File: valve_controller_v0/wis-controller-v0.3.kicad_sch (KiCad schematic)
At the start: 45 parts, among them J3 USB_C_Receptacle_USB2.0, J5 SWD, J6 JST-2PH, Q1 DMG3415UQ-7, SW1 RESET, SW4 BOOT, U1 RAK3172, U10 BAT_Positive, U11 XKB5858-Z-F-75, U2 CH340E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

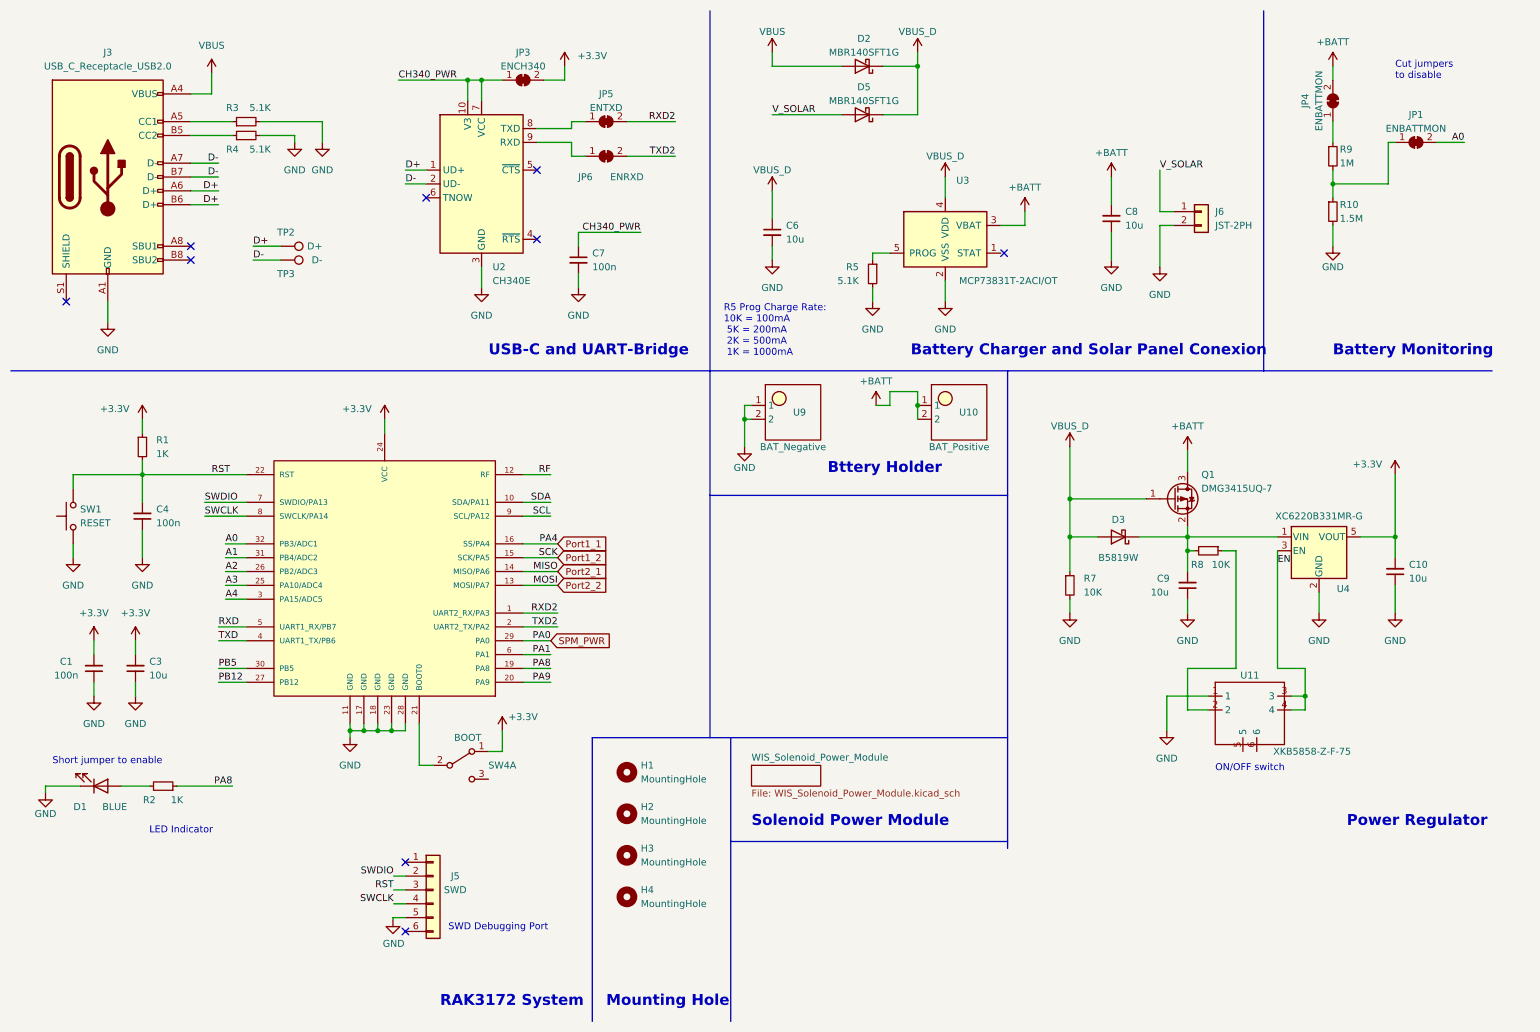
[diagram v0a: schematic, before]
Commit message: Replaced battery charger and battery holder
- Replaced battery charger to support the  new solar panel
- Replaced the battery holder by a plastic enclosure one
- Reconnected the on/off switch to avoid putting EN pin floating temporarly whne swithced
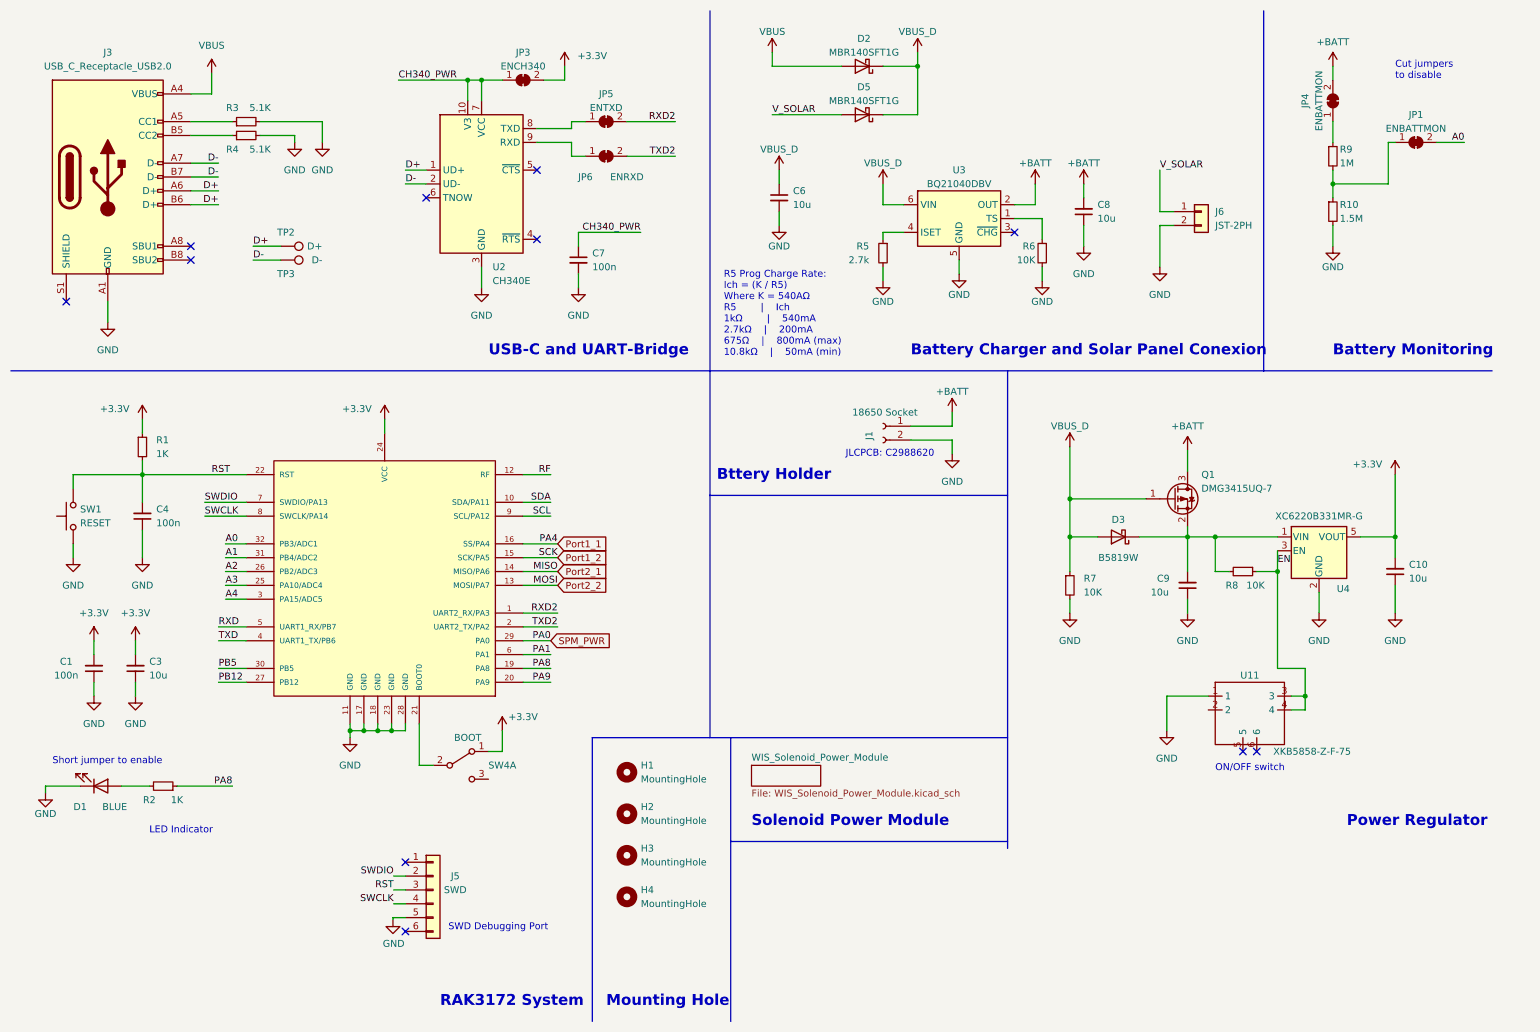
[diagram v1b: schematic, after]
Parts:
- removed U10: BAT_Positive, WIS_Solenoid_Power_module:Battery_holder_18650, symbol WISFLOW_Symbols:Battery_holder_side
- removed U3: MCP73831T-2ACI/OT, Package_TO_SOT_SMD:SOT-23-5, symbol Battery_Management:MCP73831-2-OT
- removed U9: BAT_Negative, WIS_Solenoid_Power_module:Battery_holder_18650, symbol WISFLOW_Symbols:Battery_holder_side
- added J1: 18650 Socket, Wisflow:18650_SMD, symbol Connector:Conn_01x02_Socket
- added R6: 10K, Resistor_SMD:R_0603_1608Metric, symbol Device:R_Small
- added U3: BQ21040DBV, Package_TO_SOT_SMD:SOT-23-6, symbol Battery_Management:BQ21040DBV
- R5: value 5.1K -> 2.7k
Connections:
- net +BATT: now also J1.1 (Pin_1), U3.2 (OUT)
- net EN: now also R8.1
- net GND: now also J1.2 (Pin_2), R6.2, U3.5 (GND)
- net VBUS_D: now also U3.6 (VIN)
- net at U11.2: no longer R8.1
- net at R5.1: now also U3.4 (ISET)
- new net: R6.1, U3.1 (TS)
- no-connect marks 9 -> 11
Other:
- note added: "JLCPCB: C2988620"
- note added: "R5 Prog Charge Rate: Ich = (K / R5) Where K = 540AΩ R5 | Ich 1kΩ | 540mA 2.7kΩ | 200mA 675Ω | 800mA (max) 10.8kΩ | 50mA (min)"
- note removed: "R5 Prog Charge Rate: 10K = 100mA 5K = 200mA 2K = 500mA 1K = 1000mA"
- moved on the sheet: C6, C8, R8

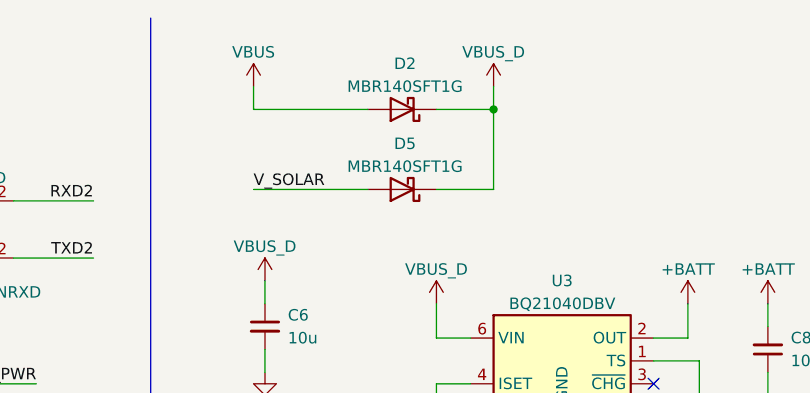
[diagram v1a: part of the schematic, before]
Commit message: Uniformized D2,D3 and D5
- Selected the same partnumber forD2, D3 and D5, all of the 1A and 40V.
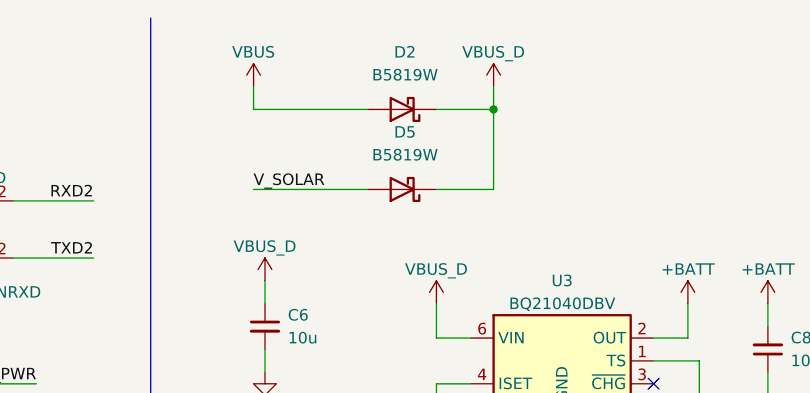
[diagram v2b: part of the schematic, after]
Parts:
- D2, D5: value MBR140SFT1G -> B5819W; footprint WIS_Solenoid_Power_module:D_MBR140SF -> Diode_SMD:D_SOD-123
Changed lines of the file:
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@@
 		(fields_autoplaced yes)
 		(property "Reference" "D2"
-			(at 169.2275 17.78 0)
-			(effects
-				(font
-					(size 1.27 1.27)
-				)
-			)
-		)
-		(property "Value" "MBR140SFT1G"
-			(at 169.2275 20.32 0)
-			(effects
-				(font
-					(size 1.27 1.27)
-				)
-			)
-		)
-		(property "Footprint" "WIS_Solenoid_Power_module:D_MBR140SF"
+			(at 169.2275 16.51 0)
+			(effects
+				(font
+					(size 1.27 1.27)
+				)
+			)
+		)
+		(property "Value" "B5819W"
+			(at 169.2275 19.05 0)
+			(effects
+				(font
+					(size 1.27 1.27)
+				)
+			)
+		)
+		(property "Footprint" "Diode_SMD:D_SOD-123"
 			(at 168.91 27.94 0)
 			(effects
@@
 		(fields_autoplaced yes)
 		(property "Reference" "D5"
-			(at 169.2275 26.67 0)
-			(effects
-				(font
-					(size 1.27 1.27)
-				)
-			)
-		)
-		(property "Value" "MBR140SFT1G"
-			(at 169.2275 29.21 0)
-			(effects
-				(font
-					(size 1.27 1.27)
-				)
-			)
-		)
-		(property "Footprint" "WIS_Solenoid_Power_module:D_MBR140SF"
+			(at 169.2275 25.4 0)
+			(effects
+				(font
+					(size 1.27 1.27)
+				)
+			)
+		)
+		(property "Value" "B5819W"
+			(at 169.2275 27.94 0)
+			(effects
+				(font
+					(size 1.27 1.27)
+				)
+			)
+		)
+		(property "Footprint" "Diode_SMD:D_SOD-123"
 			(at 168.91 36.83 0)
 			(effects

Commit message: Updated the 18650 battery holder
Changed the battery holder for the 18650 battery. Created new footprint and updated the PCB layout. Added cutouts for zip-ties
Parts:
- J1: footprint Wisflow:18650_SMD -> Wisflow:BatteryHolder_MPD_BK-18650-PC2
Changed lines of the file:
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@@
 			)
 		)
-		(property "Footprint" "Wisflow:18650_SMD"
+		(property "Footprint" "Wisflow:BatteryHolder_MPD_BK-18650-PC2"
 			(at 172.72 88.9 0)
 			(effects
